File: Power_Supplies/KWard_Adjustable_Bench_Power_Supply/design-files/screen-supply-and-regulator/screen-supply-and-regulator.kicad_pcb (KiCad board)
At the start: 2 copper layers, 156.2 x 102.9 mm, 42 parts, among them J1 B+_120Vac, J2 Pass Tube Array, J3 Meters, J4 To Panel Jacks, Q1 STP18N55M5, SW1 I-meter bypass, SW2 DUT discharge, U1 LM317

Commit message: Fix hilarious layout mistake -- swap the locations of C1 and C2.  No functional difference, but it's what I originally intended, and is a little more intuitive.
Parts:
- moved C1 27.9 mm to (92.7, 60.3)
- moved C2 27.9 mm to (120.7, 60.3)
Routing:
- net Net-(C2-Pad1): track 125.2 -> 102.7 mm
- net Net-(C1-Pad1): track 43.1 -> 29.8 mm
- net Net-(C1-Pad2): track 265.3 -> 266.2 mm

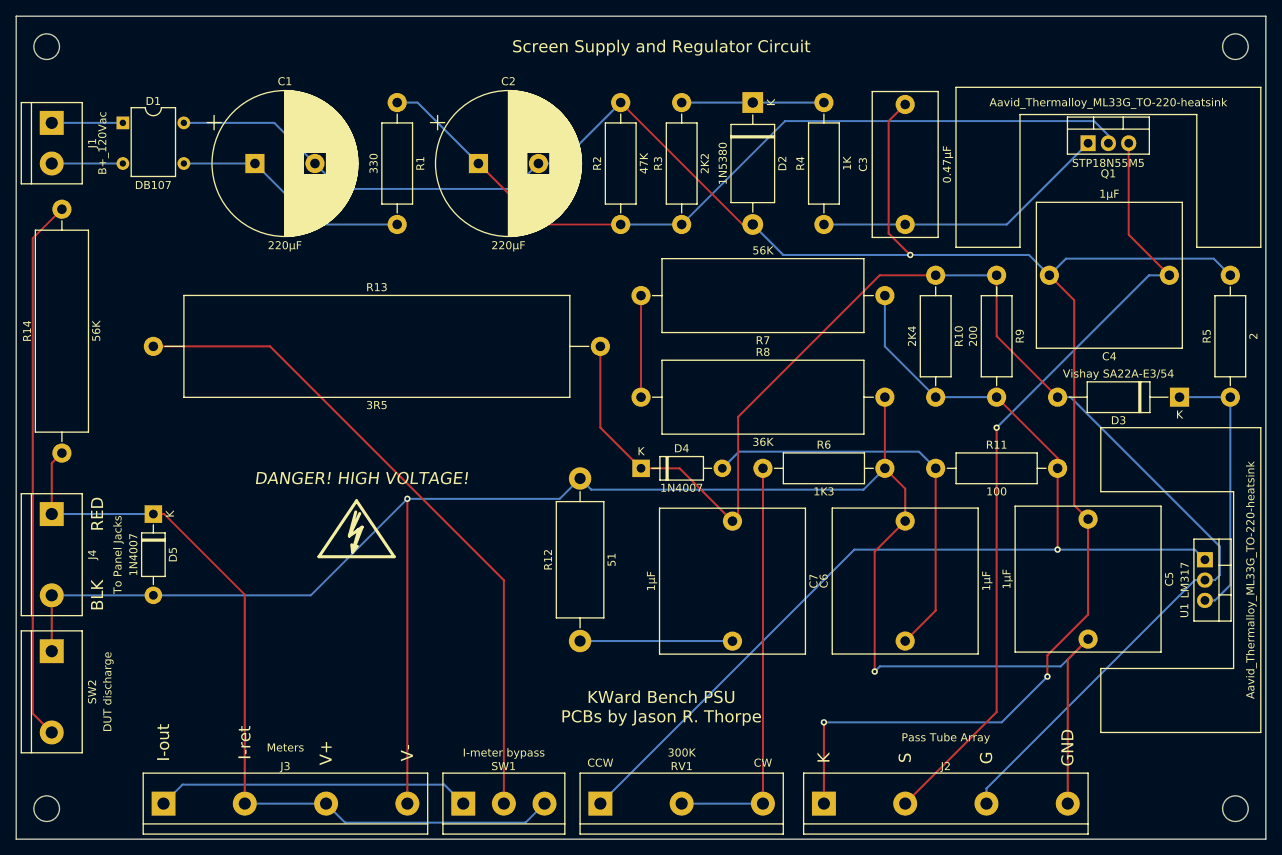
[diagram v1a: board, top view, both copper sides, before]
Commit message: Move screw terminal labels further away from footprints to reduce the change they'll be obscrured by the terminal block.
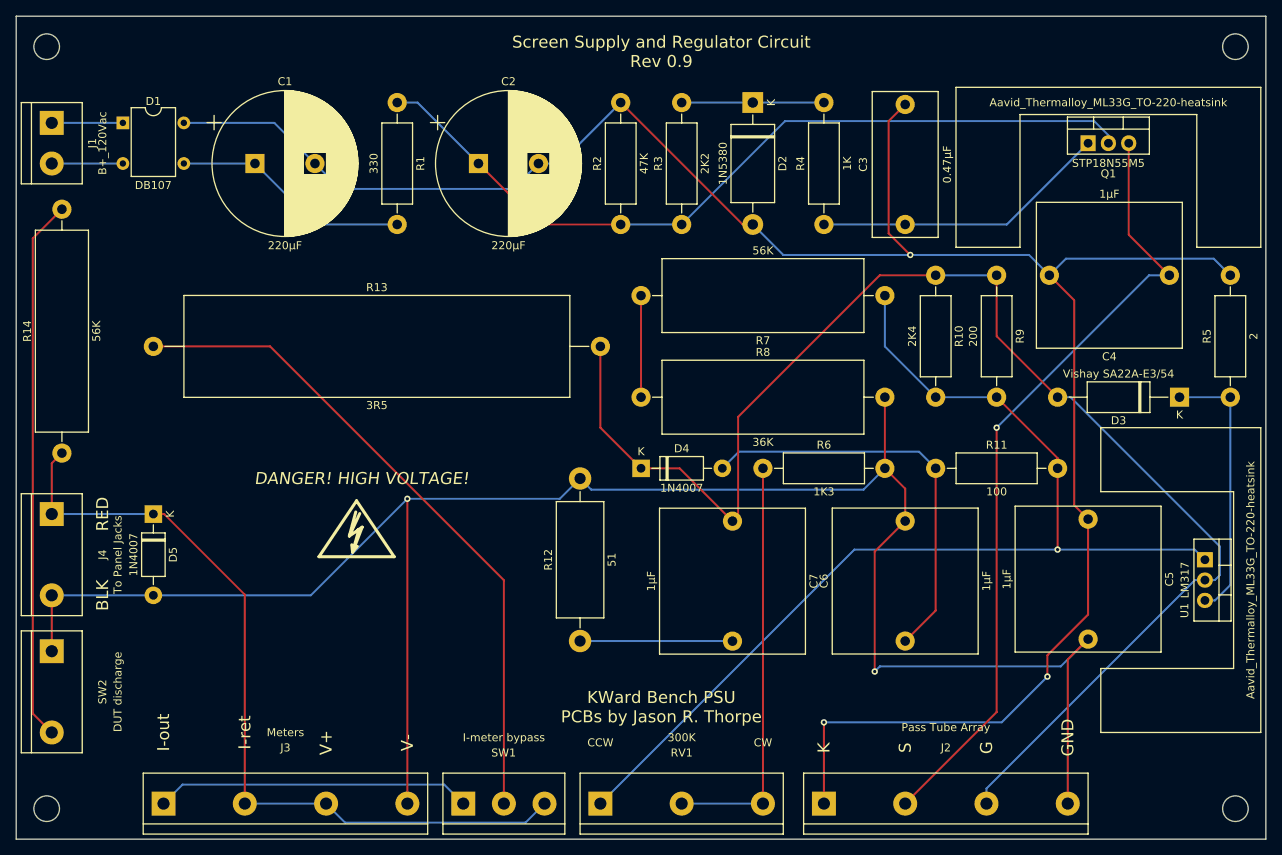
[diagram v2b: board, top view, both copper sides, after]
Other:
- board text added: "Screen Supply and Regulator Circuit Rev 0.9"
- board text removed: "Screen Supply and Regulator Circuit"
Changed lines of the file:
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@@
     (descr "simple 3-pin terminal block, pitch 10.16mm, 600V")
     (tags "terminal block bornier3")
-    (fp_text reference J2 (at 0 -4.65) (layer F.SilkS)
-      (effects (font (size 1 1) (thickness 0.15)))
-    )
-    (fp_text value "Pass Tube Array" (at 0 -8.255) (layer F.SilkS)
+    (fp_text reference J2 (at 0 -6.985) (layer F.SilkS)
+      (effects (font (size 1 1) (thickness 0.15)))
+    )
+    (fp_text value "Pass Tube Array" (at 0 -9.525) (layer F.SilkS)
       (effects (font (size 1 1) (thickness 0.15)))
     )
@@
     (descr "simple 3-pin terminal block, pitch 10.16mm, 600V")
     (tags "terminal block bornier3")
-    (fp_text reference J3 (at 0 -4.65) (layer F.SilkS)
-      (effects (font (size 1 1) (thickness 0.15)))
-    )
-    (fp_text value Meters (at 0 -6.985) (layer F.SilkS)
+    (fp_text reference J3 (at 0 -6.985) (layer F.SilkS)
+      (effects (font (size 1 1) (thickness 0.15)))
+    )
+    (fp_text value Meters (at 0 -8.89) (layer F.SilkS)
       (effects (font (size 1 1) (thickness 0.15)))
     )
@@
     (descr "simple 2-pin terminal block, pitch 5.08mm, revamped version of bornier2")
     (tags "terminal block bornier2")
-    (fp_text reference J4 (at 5.08 -5.08 90) (layer F.SilkS)
+    (fp_text reference J4 (at 5.08 -6.35 90) (layer F.SilkS)
       (effects (font (size 1 1) (thickness 0.15)))
     )
@@
     (descr "simple 3-pin terminal block, pitch 10.16mm, 600V")
     (tags "terminal block bornier3")
-    (fp_text reference RV1 (at 10.16 -4.65) (layer F.SilkS)
-      (effects (font (size 1 1) (thickness 0.15)))
-    )
-    (fp_text value 300K (at 10.16 -6.35) (layer F.SilkS)
+    (fp_text reference RV1 (at 10.16 -6.35) (layer F.SilkS)
+      (effects (font (size 1 1) (thickness 0.15)))
+    )
+    (fp_text value 300K (at 10.16 -8.255) (layer F.SilkS)
       (effects (font (size 1 1) (thickness 0.15)))
     )
@@
     (descr "simple 3-pin terminal block, pitch 5.08mm, revamped version of bornier3")
     (tags "terminal block bornier3")
-    (fp_text reference SW1 (at 5.05 -4.65) (layer F.SilkS)
-      (effects (font (size 1 1) (thickness 0.15)))
-    )
-    (fp_text value "I-meter bypass" (at 5.08 -6.35) (layer F.SilkS)
+    (fp_text reference SW1 (at 5.05 -6.35) (layer F.SilkS)
+      (effects (font (size 1 1) (thickness 0.15)))
+    )
+    (fp_text value "I-meter bypass" (at 5.08 -8.255) (layer F.SilkS)
       (effects (font (size 1 1) (thickness 0.15)))
     )
@@
     (descr "simple 2-pin terminal block, pitch 5.08mm, revamped version of bornier2")
     (tags "terminal block bornier2")
-    (fp_text reference SW2 (at 5.08 -5.08 90) (layer F.SilkS)
-      (effects (font (size 1 1) (thickness 0.15)))
-    )
-    (fp_text value "DUT discharge" (at 5.08 -6.985 90) (layer F.SilkS)
+    (fp_text reference SW2 (at 5.08 -6.35 90) (layer F.SilkS)
+      (effects (font (size 1 1) (thickness 0.15)))
+    )
+    (fp_text value "DUT discharge" (at 5.08 -8.255 90) (layer F.SilkS)
       (effects (font (size 1 1) (thickness 0.15)))
     )
@@
     (effects (font (size 1.5 1.5) (thickness 0.3)))
   )
-  (gr_text GND (at 194.31 133.35 90) (layer F.SilkS)
-    (effects (font (size 1.5 1.5) (thickness 0.3)))
-  )
-  (gr_text G (at 184.15 134.62 90) (layer F.SilkS)
-    (effects (font (size 1.5 1.5) (thickness 0.3)))
-  )
-  (gr_text S (at 173.99 134.62 90) (layer F.SilkS)
-    (effects (font (size 1.5 1.5) (thickness 0.3)))
-  )
-  (gr_text K (at 163.83 134.62 90) (layer F.SilkS)
-    (effects (font (size 1.5 1.5) (thickness 0.3)))
-  )
-  (gr_text "Screen Supply and Regulator Circuit" (at 143.51 45.72) (layer F.SilkS)
+  (gr_text GND (at 194.31 132.08 90) (layer F.SilkS)
+    (effects (font (size 1.5 1.5) (thickness 0.3)))
+  )
+  (gr_text G (at 184.15 133.35 90) (layer F.SilkS)
+    (effects (font (size 1.5 1.5) (thickness 0.3)))
+  )
+  (gr_text S (at 173.99 133.35 90) (layer F.SilkS)
+    (effects (font (size 1.5 1.5) (thickness 0.3)))
+  )
+  (gr_text K (at 163.83 133.35 90) (layer F.SilkS)
+    (effects (font (size 1.5 1.5) (thickness 0.3)))
+  )
+  (gr_text "Screen Supply and Regulator Circuit\nRev 0.9" (at 143.51 46.355) (layer F.SilkS)
     (effects (font (size 1.5 1.5) (thickness 0.3)))
   )
@@
     (effects (font (size 1.5 1.5) (thickness 0.3) italic))
   )
-  (gr_text V- (at 111.76 133.985 90) (layer F.SilkS)
-    (effects (font (size 1.5 1.5) (thickness 0.3)))
-  )
-  (gr_text V+ (at 101.6 133.985 90) (layer F.SilkS)
-    (effects (font (size 1.5 1.5) (thickness 0.3)))
-  )
-  (gr_text I-ret (at 91.44 132.715 90) (layer F.SilkS)
-    (effects (font (size 1.5 1.5) (thickness 0.3)))
-  )
-  (gr_text I-out (at 81.28 132.715 90) (layer F.SilkS)
-    (effects (font (size 1.5 1.5) (thickness 0.3)))
-  )
-  (gr_text BLK (at 73.025 114.3 90) (layer F.SilkS)
-    (effects (font (size 1.5 1.5) (thickness 0.3)))
-  )
-  (gr_text RED (at 73.025 104.14 90) (layer F.SilkS)
-    (effects (font (size 1.5 1.5) (thickness 0.3)))
-  )
-  (gr_text CW (at 156.21 135.255) (layer F.SilkS)
+  (gr_text V- (at 111.76 132.715 90) (layer F.SilkS)
+    (effects (font (size 1.5 1.5) (thickness 0.3)))
+  )
+  (gr_text V+ (at 101.6 132.715 90) (layer F.SilkS)
+    (effects (font (size 1.5 1.5) (thickness 0.3)))
+  )
+  (gr_text I-ret (at 91.44 131.445 90) (layer F.SilkS)
+    (effects (font (size 1.5 1.5) (thickness 0.3)))
+  )
+  (gr_text I-out (at 81.28 131.445 90) (layer F.SilkS)
+    (effects (font (size 1.5 1.5) (thickness 0.3)))
+  )
+  (gr_text BLK (at 73.66 114.3 90) (layer F.SilkS)
+    (effects (font (size 1.5 1.5) (thickness 0.3)))
+  )
+  (gr_text RED (at 73.66 104.14 90) (layer F.SilkS)
+    (effects (font (size 1.5 1.5) (thickness 0.3)))
+  )
+  (gr_text CW (at 156.21 132.715) (layer F.SilkS)
     (effects (font (size 1 1) (thickness 0.15)))
   )
-  (gr_text CCW (at 135.89 135.255) (layer F.SilkS)
+  (gr_text CCW (at 135.89 132.715) (layer F.SilkS)
     (effects (font (size 1 1) (thickness 0.15)))
   )
